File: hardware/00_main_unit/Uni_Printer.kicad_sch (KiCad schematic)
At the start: 9 parts, among them J5 FIDUCIAL, J6 FIDUCIAL

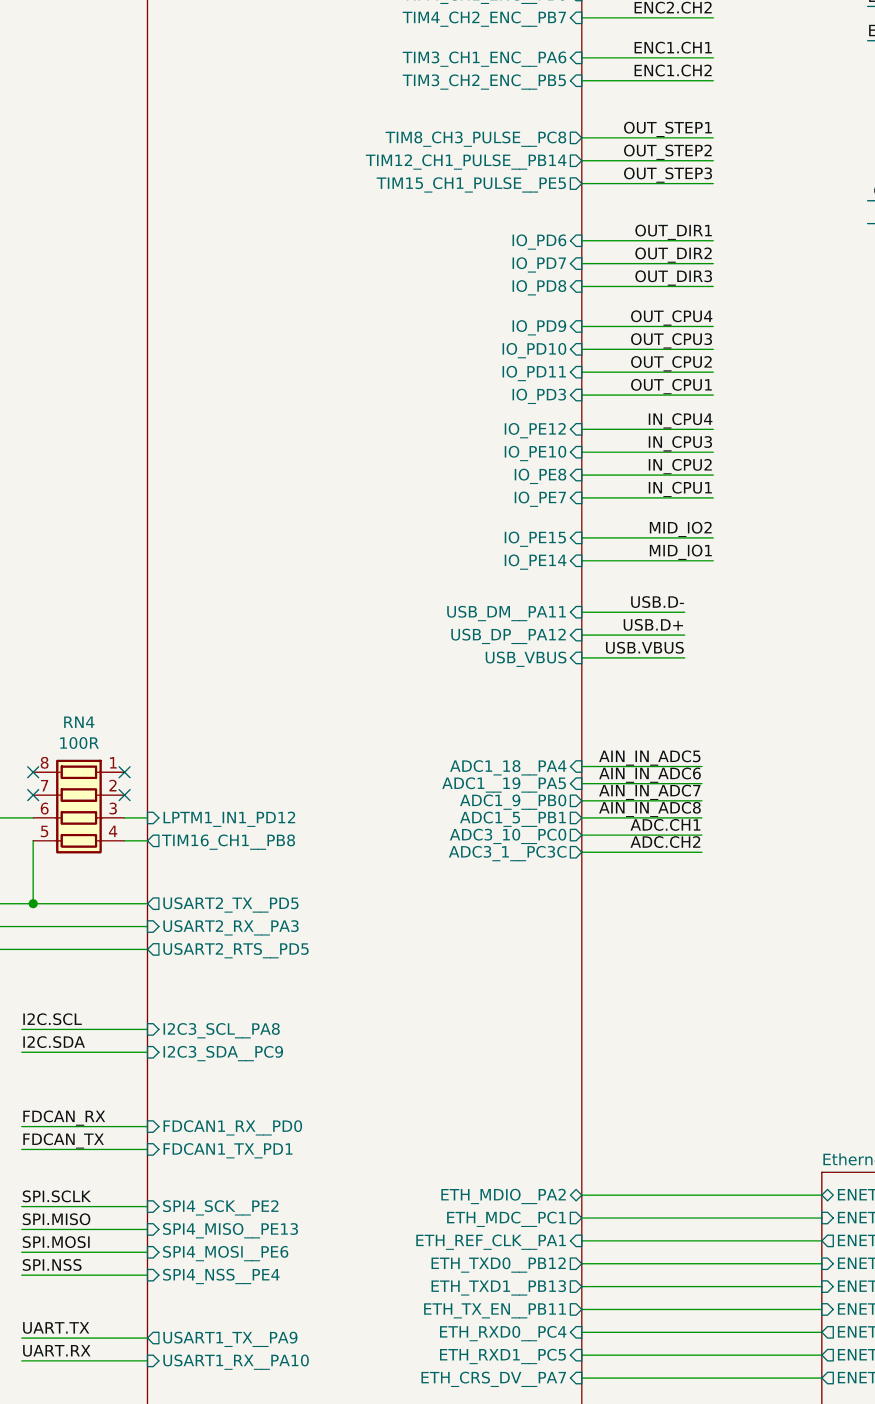
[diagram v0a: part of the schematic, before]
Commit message: Fixes after wrong merge
Signed-off-by: Jacek <matuszewski.kartech@gmail.com>
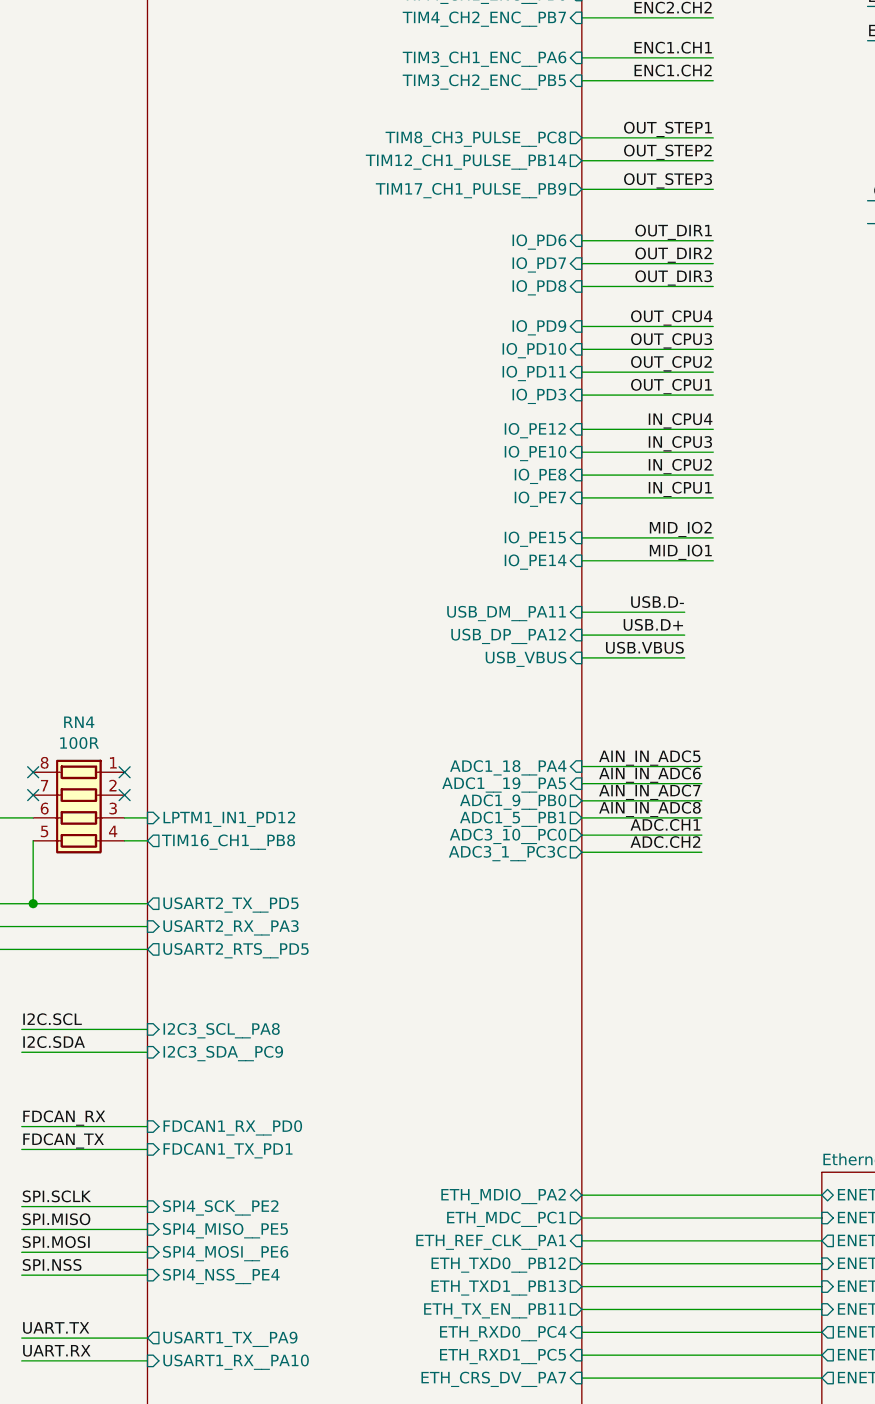
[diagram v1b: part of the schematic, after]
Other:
- sheet Processor ports: added SPI4_MISO__PE5, TIM17_CH1_PULSE__PB9; removed SPI4_MISO__PE13, TIM15_CH1_PULSE__PE5
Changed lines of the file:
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@@
     (stroke (width 0) (type solid) (color 0 0 0 0))
   )
-  (wire (pts (xy 97.79 159.385) (xy 112.395 159.385))
+  (wire (pts (xy 97.79 160.02) (xy 112.395 160.02))
     (stroke (width 0) (type solid) (color 0 0 0 0))
   )
@@
     (effects (font (size 1.27 1.27)) (justify right bottom))
   )
-  (label "OUT_STEP3" (at 112.395 159.385 180)
+  (label "OUT_STEP3" (at 112.395 160.02 180)
     (effects (font (size 1.27 1.27)) (justify right bottom))
   )
@@
       (effects (font (size 1.27 1.27)) (justify left))
     )
-    (pin "SPI4_MISO__PE13" input (at 49.53 275.59 180)
-      (effects (font (size 1.27 1.27)) (justify left))
-    )
     (pin "SPI4_MOSI__PE6" input (at 49.53 278.13 180)
       (effects (font (size 1.27 1.27)) (justify left))
@@
       (effects (font (size 1.27 1.27)) (justify right))
     )
-    (pin "TIM15_CH1_PULSE__PE5" output (at 97.79 159.385 0)
-      (effects (font (size 1.27 1.27)) (justify right))
-    )
     (pin "TIM12_CH1_PULSE__PB14" output (at 97.79 156.845 0)
       (effects (font (size 1.27 1.27)) (justify right))
@@
     (pin "NRST" input (at 97.79 81.915 0)
       (effects (font (size 1.27 1.27)) (justify right))
+    )
+    (pin "TIM17_CH1_PULSE__PB9" output (at 97.79 160.02 0)
+      (effects (font (size 1.27 1.27)) (justify right))
+    )
+    (pin "SPI4_MISO__PE5" input (at 49.53 275.59 180)
+      (effects (font (size 1.27 1.27)) (justify left))
     )
   )
@@
       (reference "#PWR0125") (unit 1) (value "GND") (footprint "")
     )
+    (path "/00000000-0000-0000-0000-00005c984242/6c7b11a9-d154-4017-ace2-520511fc73f4"
+      (reference "#PWR0166") (unit 1) (value "GND") (footprint "")
+    )
     (path "/00000000-0000-0000-0000-00005c984242/00000000-0000-0000-0000-00005e76b0e3"
       (reference "C10") (unit 1) (value "10uF") (footprint "Capacitor_SMD:C_0603_1608Metric")
@@
       (reference "J13") (unit 1) (value "Conn_01x04_Male") (footprint "Connector_PinHeader_2.54mm:PinHeader_1x04_P2.54mm_Vertical")
     )
+    (path "/00000000-0000-0000-0000-00005c984242/42bf230f-6f5e-40ce-a436-0d8181ec0de1"
+      (reference "J15") (unit 1) (value "Conn_01x06_Male") (footprint "Connector_PinHeader_2.54mm:PinHeader_1x06_P2.54mm_Vertical")
+    )
     (path "/00000000-0000-0000-0000-00005c984242/00000000-0000-0000-0000-00005c9adb60"
       (reference "R3") (unit 1) (value "2k2") (footprint "Resistor_SMD:R_0603_1608Metric")
@@
       (reference "RN8") (unit 1) (value "100R") (footprint "moje:R_Array_Convex_4x0603")
     )
+    (path "/00000000-0000-0000-0000-00005c984242/4302e786-1618-4a6d-b66d-1bbca9b12442"
+      (reference "RN11") (unit 1) (value "100R") (footprint "moje:R_Array_Convex_4x0603")
+    )
     (path "/00000000-0000-0000-0000-00005c984242/00000000-0000-0000-0000-00005c9adae2"
       (reference "SW2") (unit 1) (value "SW_Push") (footprint "Buttons_Switches_SMD:SW_SPST_B3U-1000P")
@@
       (reference "C37") (unit 1) (value "100n") (footprint "Capacitor_SMD:C_0603_1608Metric")
     )
-    (path "/00000000-0000-0000-0000-00005fc2896f/1d1e2688-e836-4b8e-8413-78f380656272"
-      (reference "C39") (unit 1) (value "2.2uF") (footprint "Capacitor_SMD:C_0603_1608Metric")
+    (path "/00000000-0000-0000-0000-00005fc2896f/0a264901-2af9-467b-a776-283d7e054ddb"
+      (reference "CP1") (unit 1) (value "2.2uF") (footprint "Capacitor_SMD:C_0603_1608Metric")
     )
     (path "/00000000-0000-0000-0000-00005fc2896f/a62c4667-75c6-4bfc-b784-f506a80a747e"
@@
       (reference "J12") (unit 1) (value "RJ45") (footprint "Connector_RJ:RJ45_Amphenol_54602-x08_Horizontal")
     )
-    (path "/6e32f2aa-aff0-4978-a4c5-4354c79bd585/fa9a855c-57eb-4941-a07d-af1c5b2a5cda"
-      (reference "J15") (unit 1) (value "Conn_01x10") (footprint "")
-    )
-    (path "/6e32f2aa-aff0-4978-a4c5-4354c79bd585/f6b01b7e-9af5-4b6d-90f8-d9fec12ef3a8"
-      (reference "J16") (unit 1) (value "Conn_01x10") (footprint "")
-    )
-    (path "/6e32f2aa-aff0-4978-a4c5-4354c79bd585/0f0faa80-d75f-4072-ba3e-1bda7be2b2d7"
-      (reference "J17") (unit 1) (value "Conn_01x10") (footprint "")
-    )
-    (path "/6e32f2aa-aff0-4978-a4c5-4354c79bd585/198ee0bf-8119-4e40-aa15-56f5a6b51b0c"
-      (reference "J18") (unit 1) (value "Conn_01x10") (footprint "")
-    )
-    (path "/6e32f2aa-aff0-4978-a4c5-4354c79bd585/bc615b1e-8aa6-4a89-9ec1-815447178a85"
-      (reference "J19") (unit 1) (value "Conn_01x10") (footprint "")
-    )
-    (path "/6e32f2aa-aff0-4978-a4c5-4354c79bd585/e993a00a-e17c-444c-a319-896bc0780eeb"
-      (reference "J20") (unit 1) (value "Conn_01x10") (footprint "")
-    )
     (path "/6e32f2aa-aff0-4978-a4c5-4354c79bd585/80b016f3-f02f-4433-9715-9f9d52c38dcd"

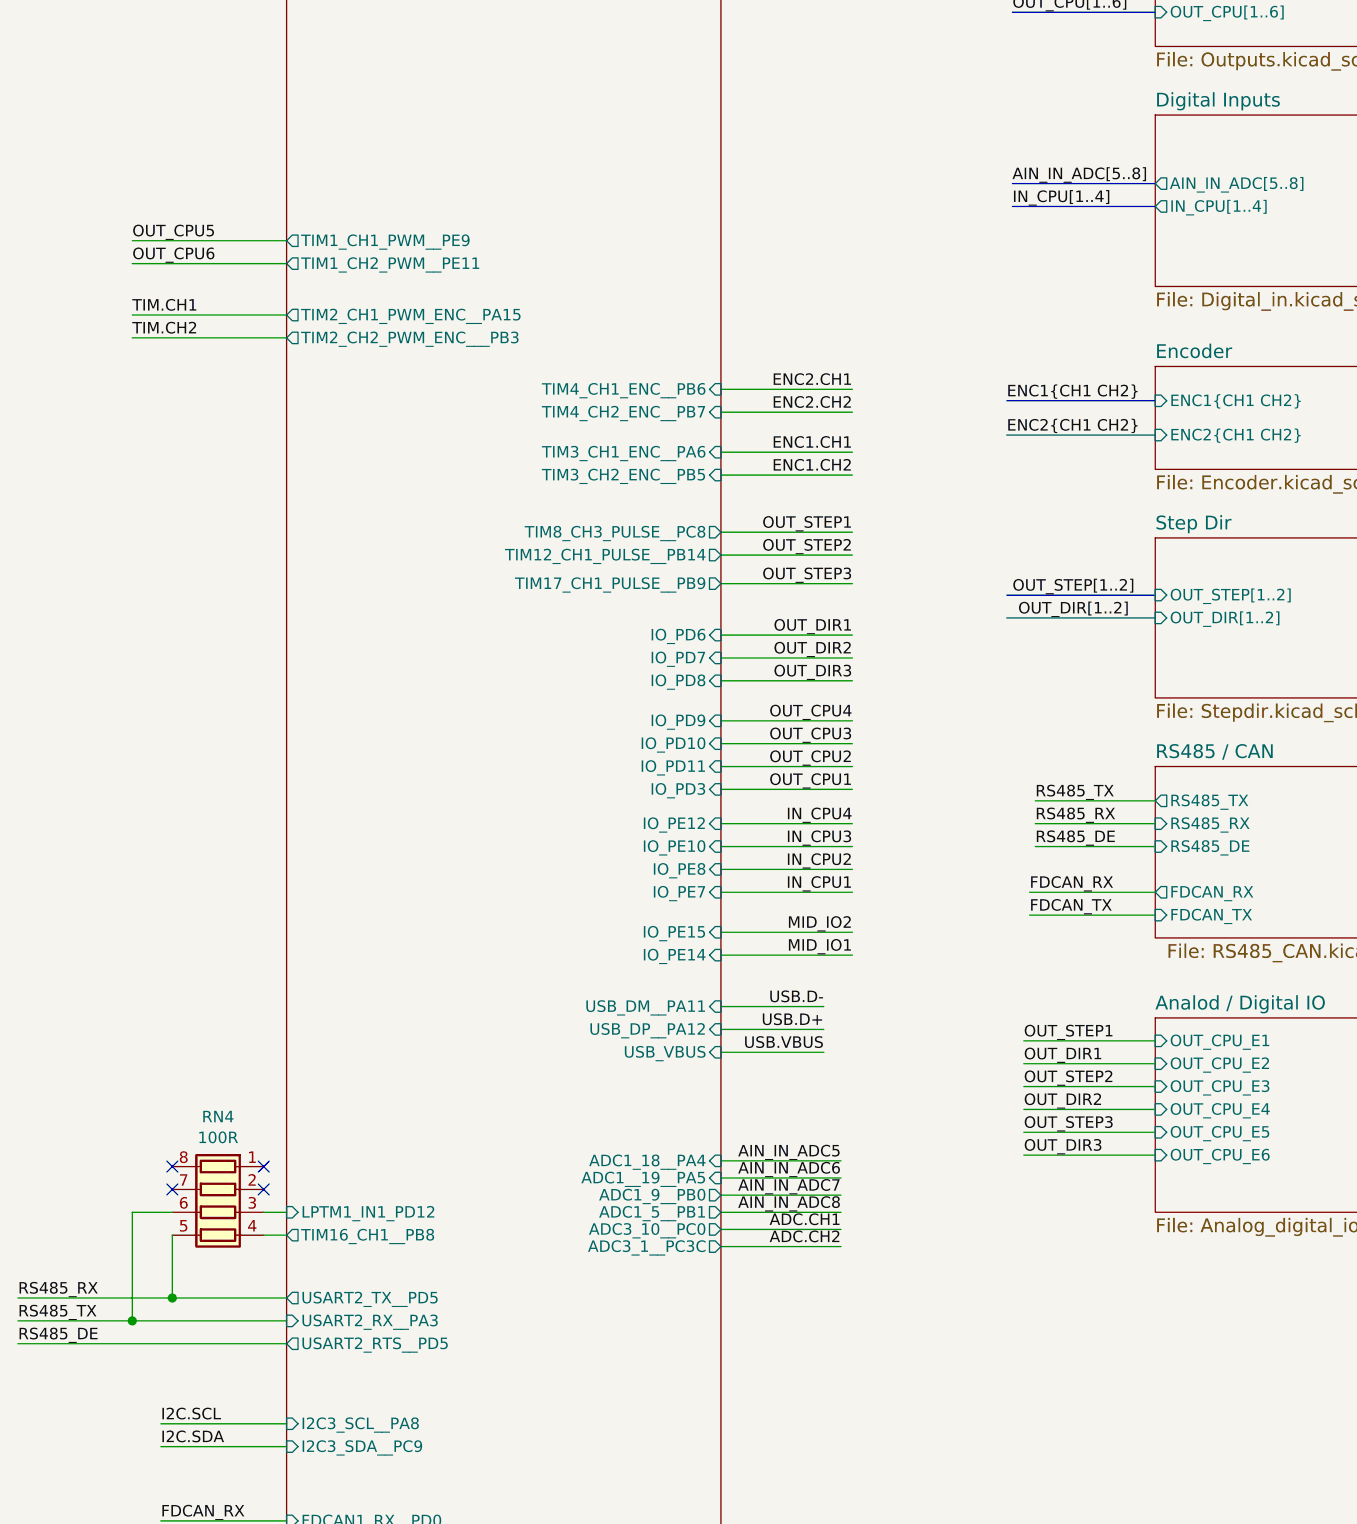
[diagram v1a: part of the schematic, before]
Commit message: Fixes for new hw version
Signed-off-by: Jarosław Karwik <jaroslaw.karwik@gmail.com>
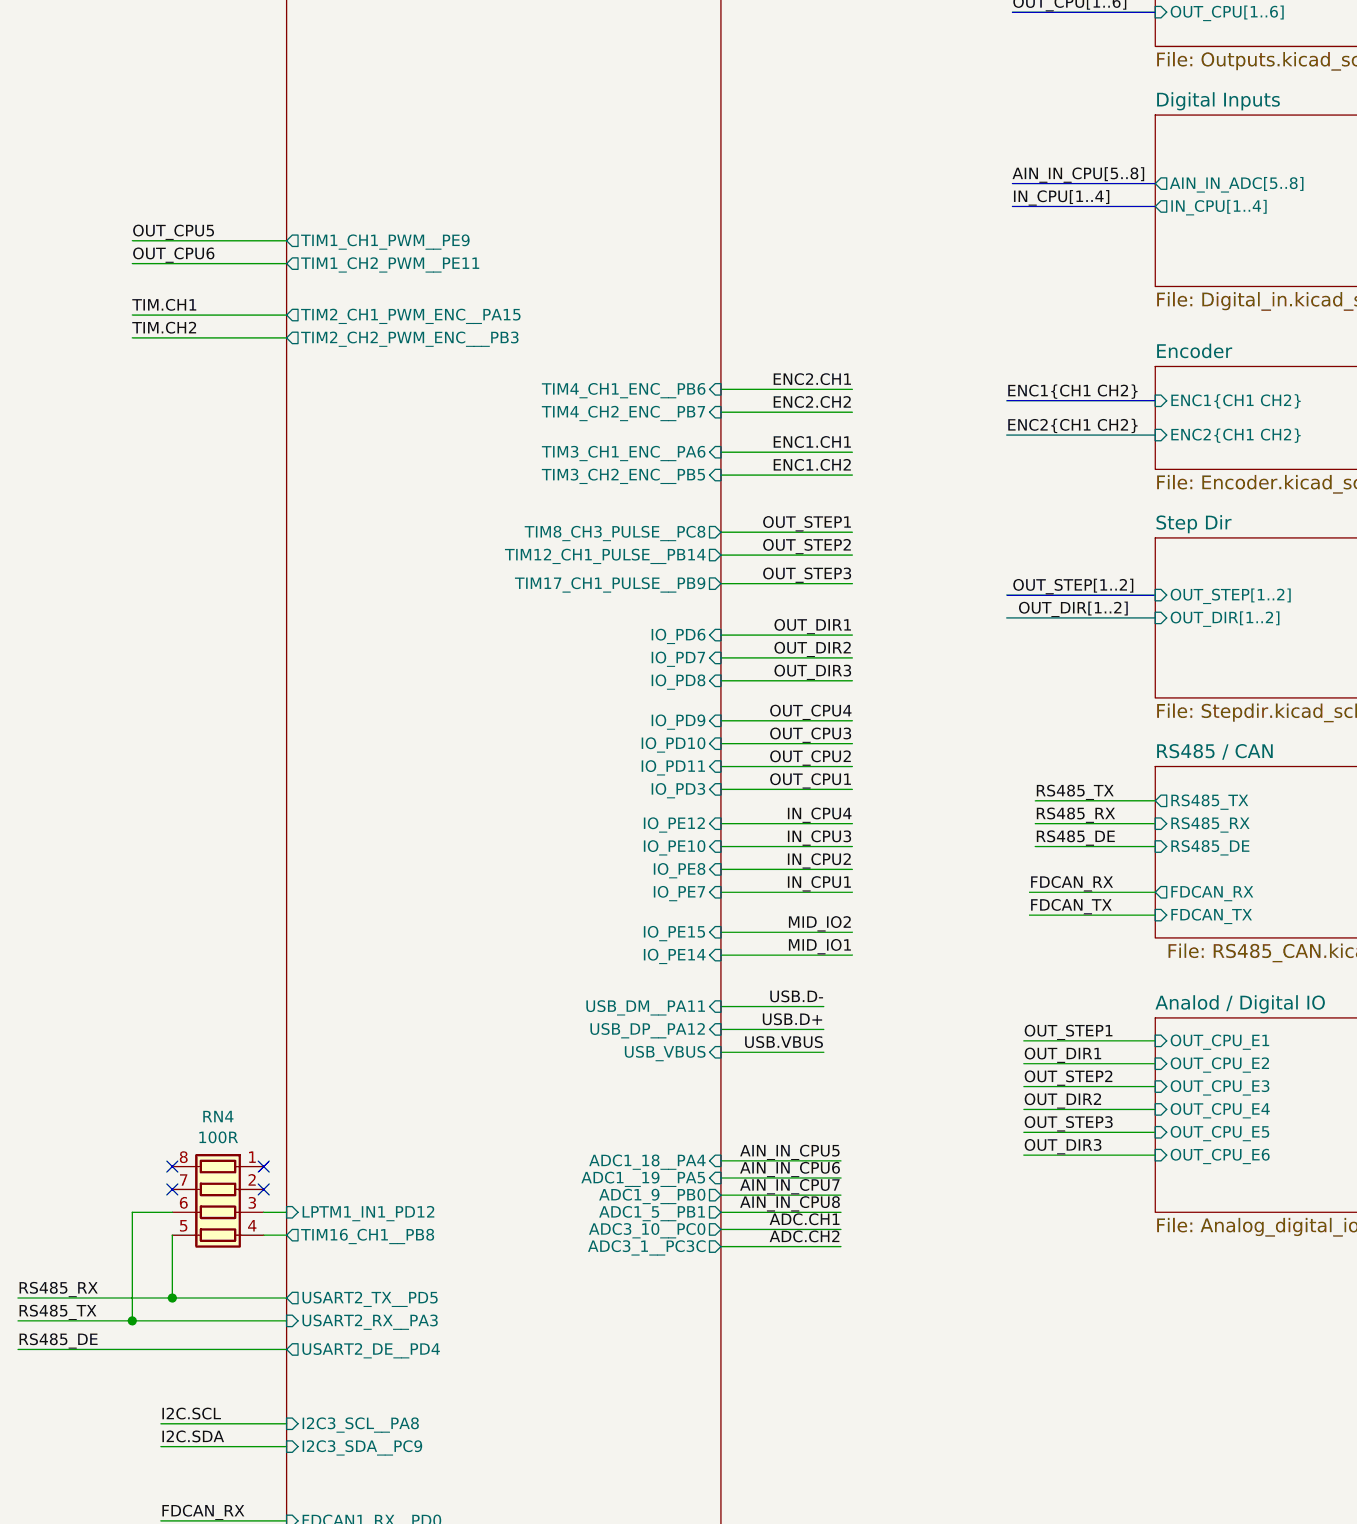
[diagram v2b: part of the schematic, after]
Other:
- sheet Processor ports: added USART2_DE__PD4; removed USART2_RTS__PD5
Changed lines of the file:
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@@
   (title_block
     (title "Uni printer")
-    (date "2020-04-30")
+    (date "2021-02-20")
     (rev "2.0")
     (company "Kartech")
@@
     (stroke (width 0) (type solid) (color 0 0 0 0))
   )
-  (wire (pts (xy 19.685 244.475) (xy 49.53 244.475))
+  (wire (pts (xy 19.685 245.11) (xy 49.53 245.11))
     (stroke (width 0) (type solid) (color 0 0 0 0))
   )
@@
     (effects (font (size 1.27 1.27)) (justify left bottom))
   )
-  (label "RS485_DE" (at 19.685 244.475 0)
+  (label "RS485_DE" (at 19.685 245.11 0)
     (effects (font (size 1.27 1.27)) (justify left bottom))
   )
@@
     (effects (font (size 1.27 1.27)) (justify right bottom))
   )
-  (label "AIN_IN_ADC5" (at 111.125 224.155 180)
-    (effects (font (size 1.27 1.27)) (justify right bottom))
-  )
-  (label "AIN_IN_ADC6" (at 111.125 226.06 180)
-    (effects (font (size 1.27 1.27)) (justify right bottom))
-  )
-  (label "AIN_IN_ADC7" (at 111.125 227.965 180)
-    (effects (font (size 1.27 1.27)) (justify right bottom))
-  )
-  (label "AIN_IN_ADC8" (at 111.125 229.87 180)
+  (label "AIN_IN_CPU5" (at 111.125 224.155 180)
+    (effects (font (size 1.27 1.27)) (justify right bottom))
+  )
+  (label "AIN_IN_CPU6" (at 111.125 226.06 180)
+    (effects (font (size 1.27 1.27)) (justify right bottom))
+  )
+  (label "AIN_IN_CPU7" (at 111.125 227.965 180)
+    (effects (font (size 1.27 1.27)) (justify right bottom))
+  )
+  (label "AIN_IN_CPU8" (at 111.125 229.87 180)
     (effects (font (size 1.27 1.27)) (justify right bottom))
   )
@@
     (effects (font (size 1.27 1.27)) (justify left bottom))
   )
-  (label "AIN_IN_ADC[5..8]" (at 130.175 115.57 0)
+  (label "AIN_IN_CPU[5..8]" (at 130.175 115.57 0)
     (effects (font (size 1.27 1.27)) (justify left bottom))
   )
@@
       (effects (font (size 1.27 1.27)) (justify left))
     )
-    (pin "USART2_RTS__PD5" output (at 49.53 244.475 180)
-      (effects (font (size 1.27 1.27)) (justify left))
-    )
     (pin "USART2_RX__PA3" input (at 49.53 241.935 180)
       (effects (font (size 1.27 1.27)) (justify left))
@@
       (effects (font (size 1.27 1.27)) (justify left))
     )
+    (pin "USART2_DE__PD4" output (at 49.53 245.11 180)
+      (effects (font (size 1.27 1.27)) (justify left))
+    )
